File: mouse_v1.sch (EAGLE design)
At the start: 56 parts, among them U1 L293DD

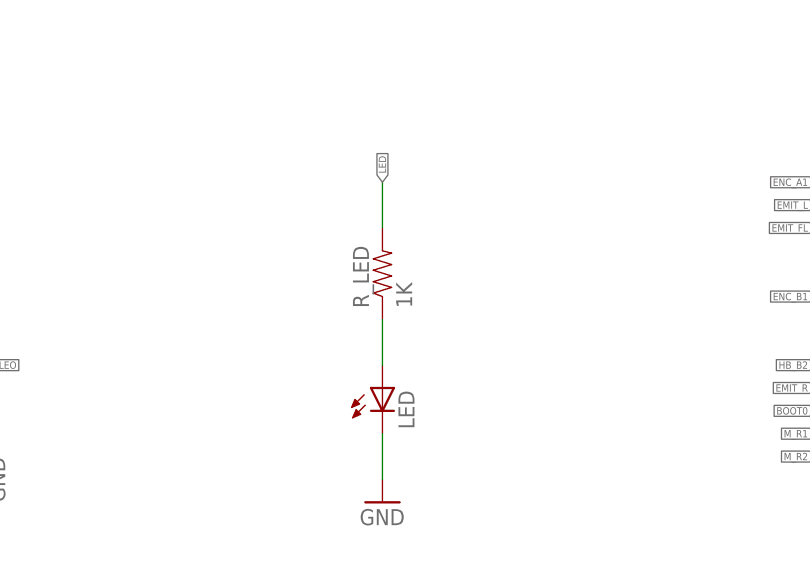
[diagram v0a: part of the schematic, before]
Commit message: LED Resistor
1000 -> 100
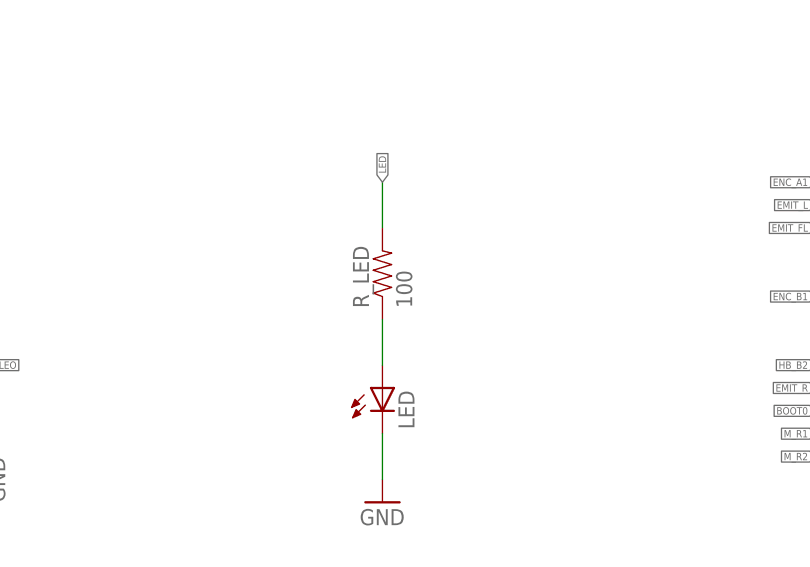
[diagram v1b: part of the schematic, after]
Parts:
- R_LED: value 1K -> 100
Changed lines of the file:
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@@
 <part name="C_3V3REG2" library="SparkFun" deviceset="CAP" device="0603-CAP" value="0.1uF"/>
 <part name="U1" library="L293DD" deviceset="L293DD" device=""/>
-<part name="R_LED" library="SparkFun-Resistors" deviceset="1.8KOHM1/10W1%(0603)" device="" value="1K"/>
+<part name="R_LED" library="SparkFun-Resistors" deviceset="1.8KOHM1/10W1%(0603)" device="" value="100"/>
 <part name="LED" library="led" library_urn="urn:adsk.eagle:library:259" deviceset="LED" device="CHIPLED_0603" package3d_urn="urn:adsk.eagle:package:15822/2"/>
 <part name="GND4" library="SparkFun" deviceset="GND" device=""/>

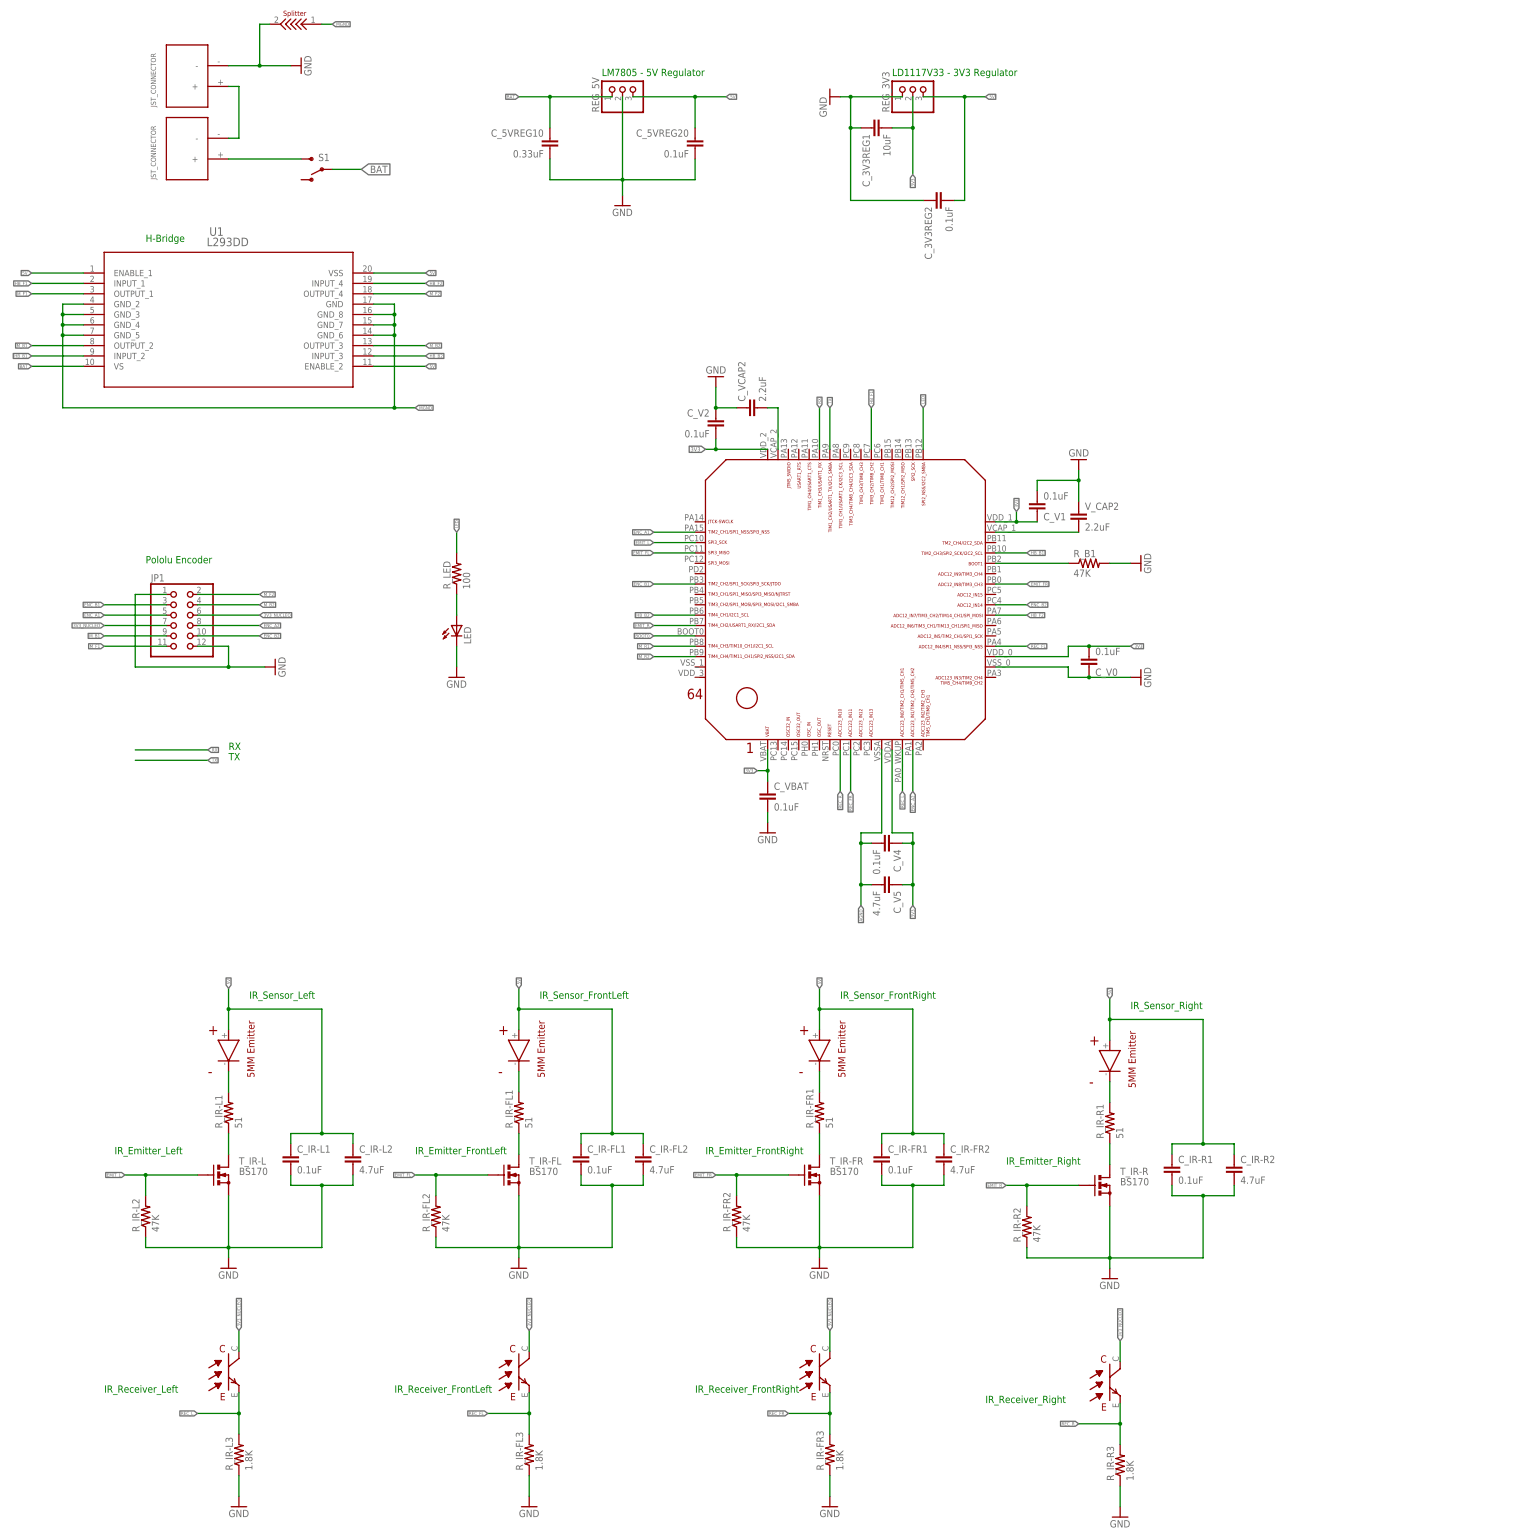
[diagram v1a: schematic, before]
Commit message: Throughput -> SMD MOSFET + REG
Added SMD mosfet and regulator libraries, and added them to the schematic in place of the old throughput parts
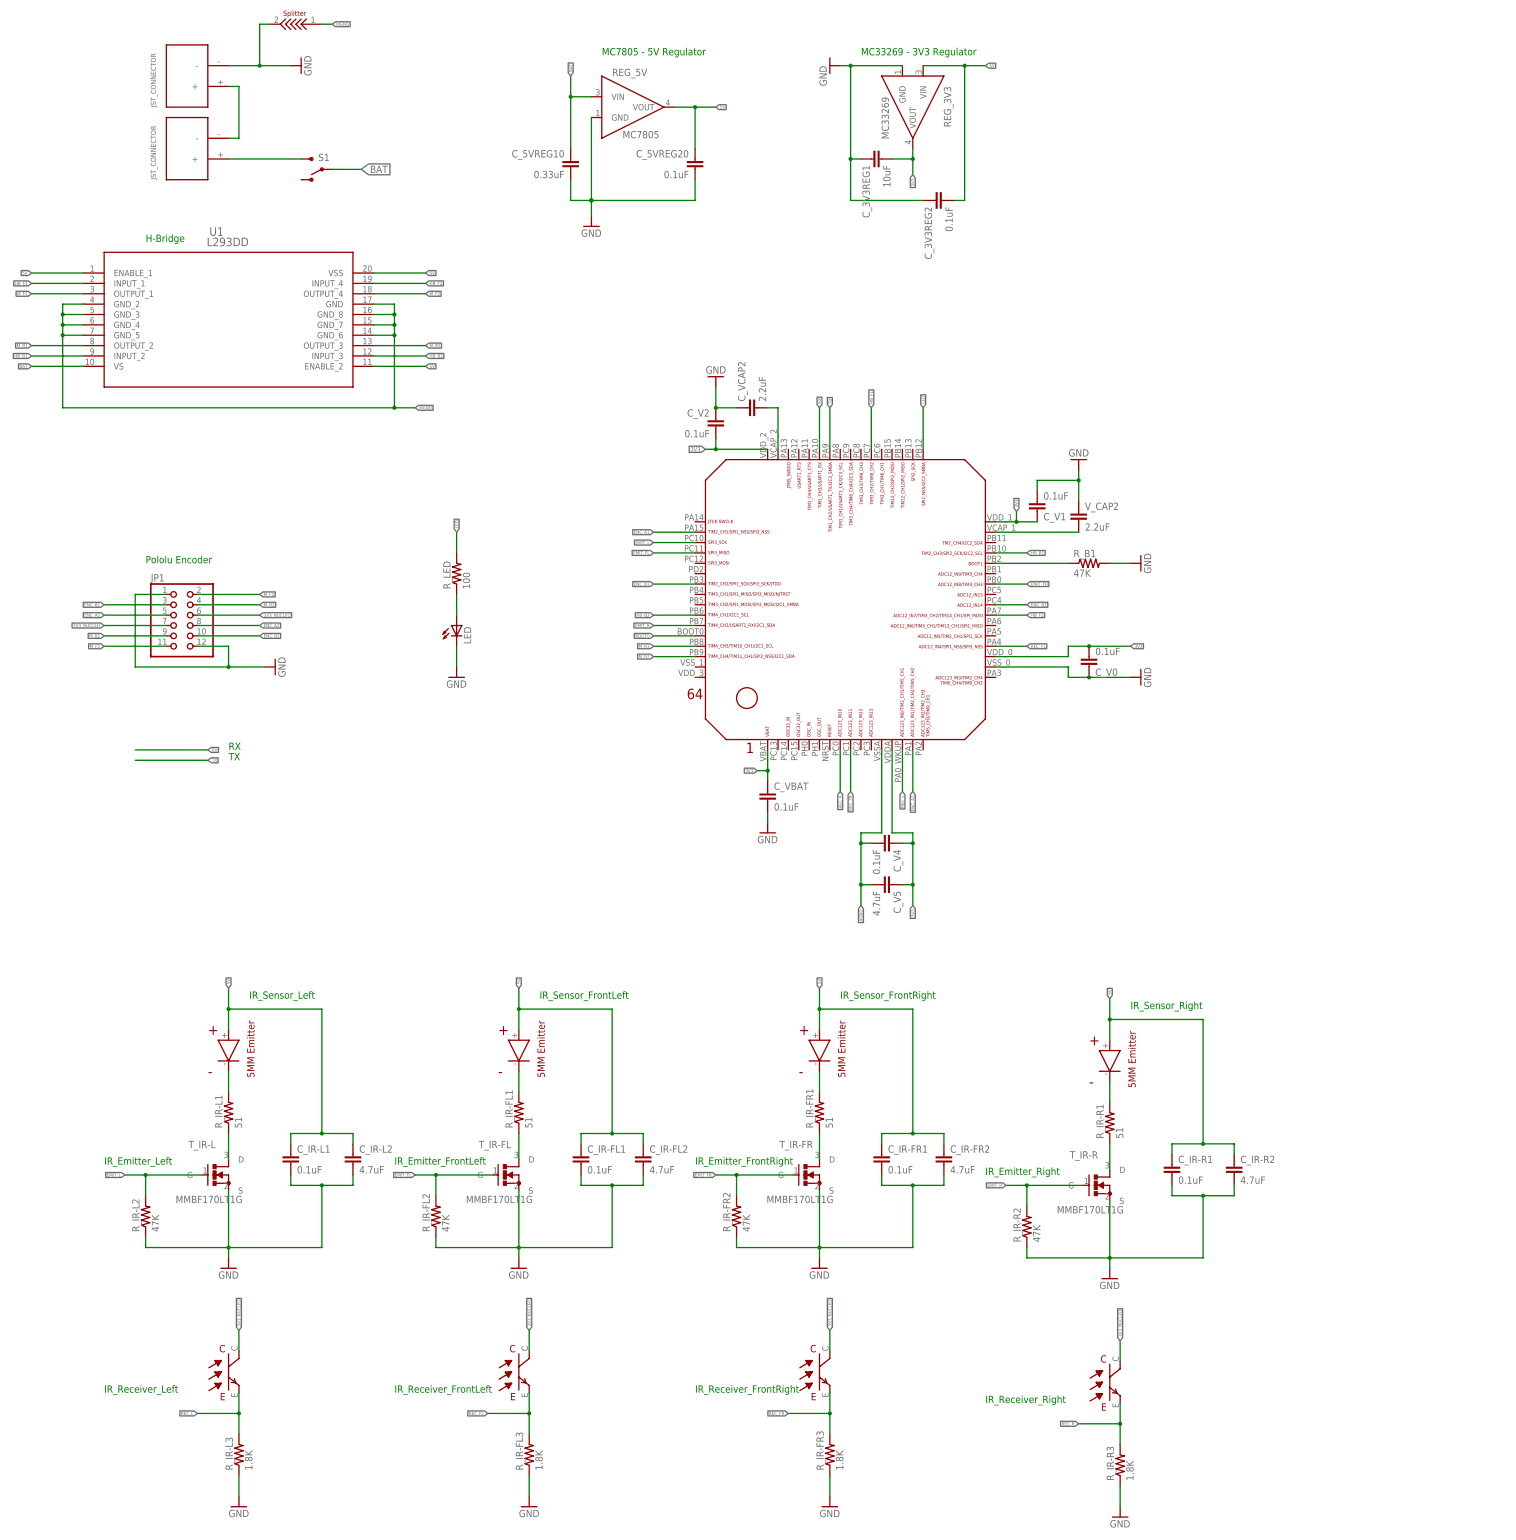
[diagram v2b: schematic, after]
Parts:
- REG_3V3: value (none) -> MC33269; device pinhead:PINHD-1X3 -> MC33269:MC33269
- REG_5V: value (none) -> MC7805; device pinhead:PINHD-1X3 -> MC33269:MC7805
- T_IR-FL, T_IR-FR, T_IR-L, T_IR-R: value BS170 -> MMBF170LT1G; device transistor-small-signal:BS170 -> MMBF170LT1:MMBF170LT1G
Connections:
- net 3V3: now also REG_3V3.VOUT; no longer REG_3V3.2
- net 5V: now also REG_3V3.VIN, REG_5V.VOUT; no longer REG_3V3.3, REG_5V.3
- net BAT: now also REG_5V.VIN; no longer REG_5V.1
- net GND: now also REG_3V3.GND, REG_5V.GND; no longer REG_3V3.1, REG_5V.2
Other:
- note added: "MC33269 - 3V3 Regulator"
- note added: "MC7805 - 5V Regulator"
- note removed: "LD1117V33 - 3V3 Regulator"
- note removed: "LM7805 - 5V Regulator"
- moved on the sheet: C_3V3REG1, C_5VREG10, C_5VREG20

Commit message: Added BOOT and NRST
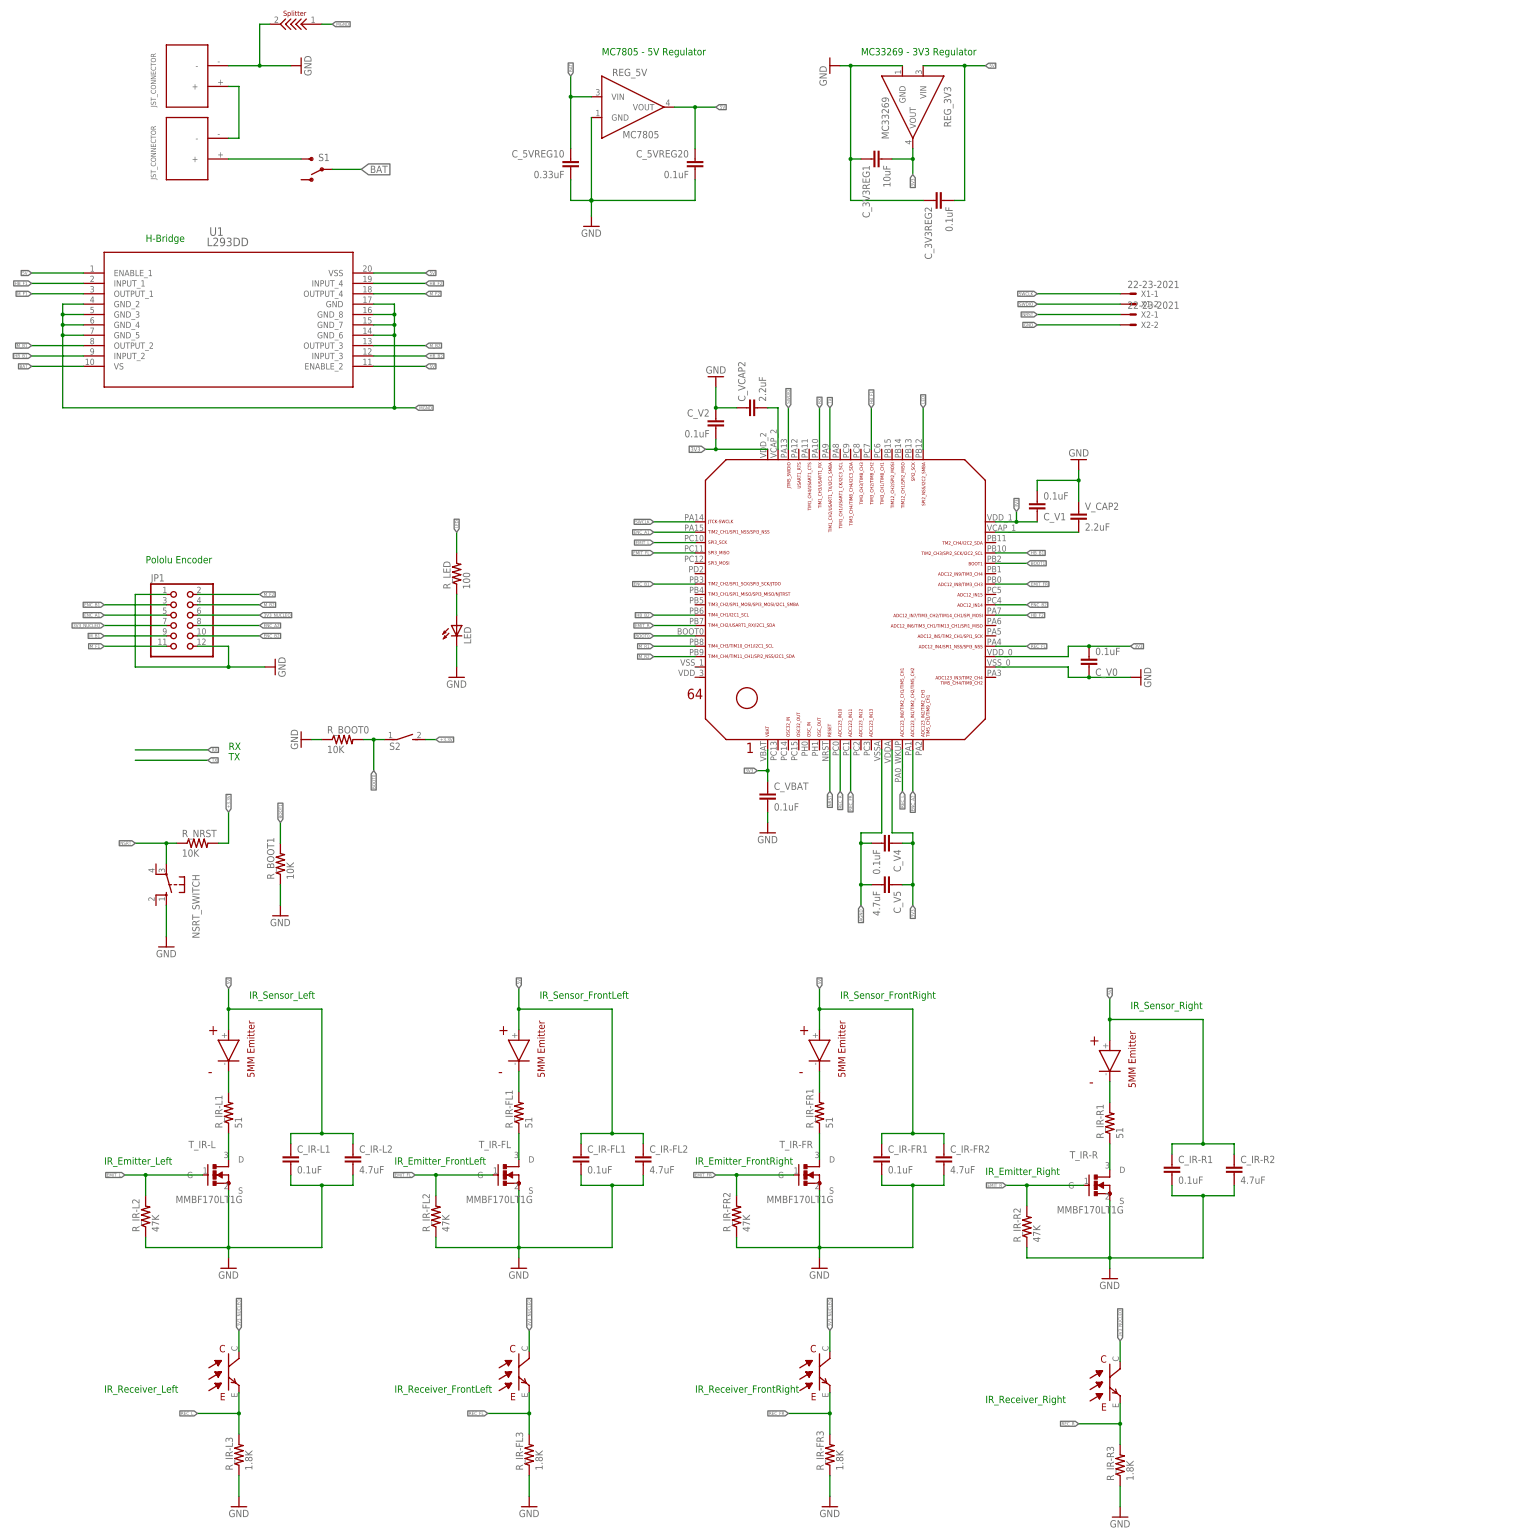
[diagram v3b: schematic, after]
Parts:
- removed R_B1: 47K, SparkFun-Resistors:1.8KOHM1/10W1%(0603)
- added NSRT_SWITCH: (no value), switch-omron:10-XX
- added R_BOOT0, R_BOOT1, R_NRST: 10K, rcl:R-US_0204/2V
- added S2: (no value), switch-dil:DS01E
- added X1, X2: 22-23-2021, con-molex:22-23-2021
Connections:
- removed net N$5: R_B1.1, U$1.PB2
- new net +3.3V: R_NRST.2, S2.2
- new net BOOT1: R_BOOT1.2, U$1.PB2
- new net N$1: R_BOOT1.1
- new net NRST: U$1.NRST, X2-1.S
- new net NSRT: NSRT_SWITCH.P, R_NRST.1
- new net SWCLK: U$1.PA14, X1-1.S
- new net SWDIO: U$1.PA13, X1-2.S
- net BOOT0: now also R_BOOT0.2, S2.1
- net GND: now also NSRT_SWITCH.S, R_BOOT0.1, X2-2.S; no longer R_B1.2
